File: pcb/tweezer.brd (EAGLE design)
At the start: 20 x 26 mm, 33 parts, among them IC1 AD7995, IC2 TS507CLT, IC3 TS507CLT, IC5 ESDA6V1SC5, IC6 AT24CS04-SOT23

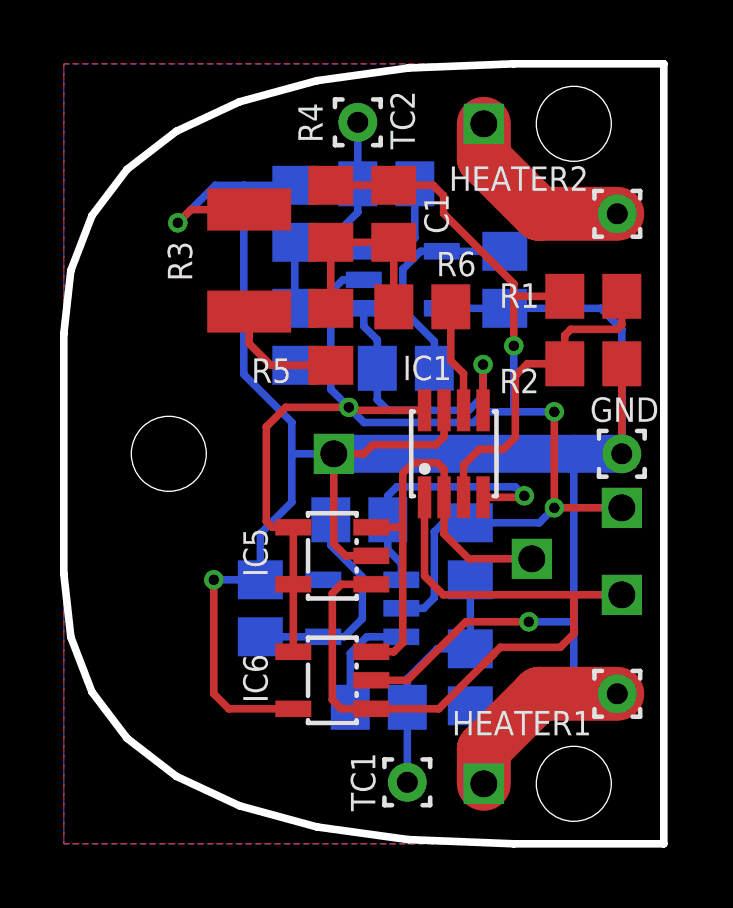
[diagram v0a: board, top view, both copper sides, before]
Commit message: reworked current path on boards and added new gerber files
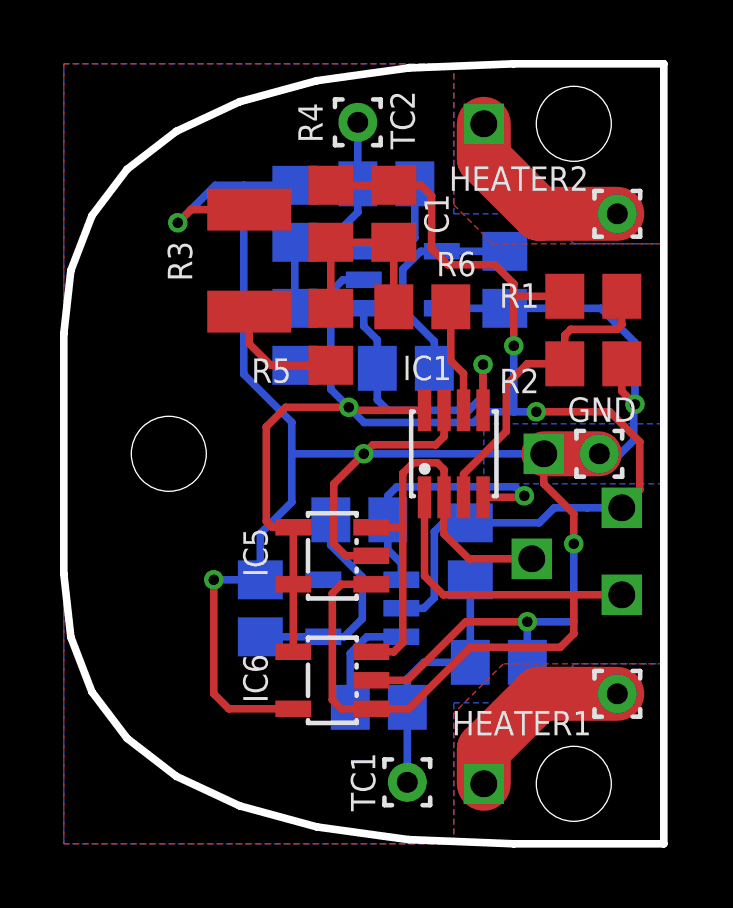
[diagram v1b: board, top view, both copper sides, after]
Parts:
- moved U$11 7.00 mm to (16.0, 13.0)
- moved C2 1.07 mm to (14.5, 6.05), turned to 180 degrees
- moved GND 0.75 mm to (17.9, 13.0)
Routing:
- net GND: track 84.0 -> 78.5 mm, vias 3 -> 6
- net +5V: track 54.6 -> 57.8 mm, vias 4 -> 3
- added copper zone on layer 1, net HEATER_1
- added copper zone on layer 16, net HEATER_1
- added copper zone on layer 1, net HEATER_2
- added copper zone on layer 16, net HEATER_2
